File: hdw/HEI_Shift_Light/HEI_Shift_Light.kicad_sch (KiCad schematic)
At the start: 0 parts

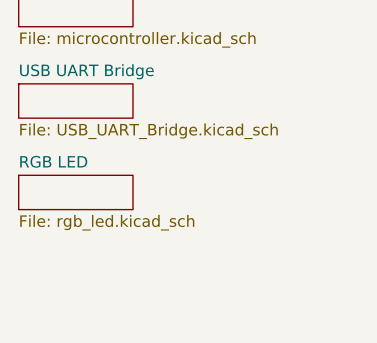
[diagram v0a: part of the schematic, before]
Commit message: moved GND connections to mount holes, updated gitignore
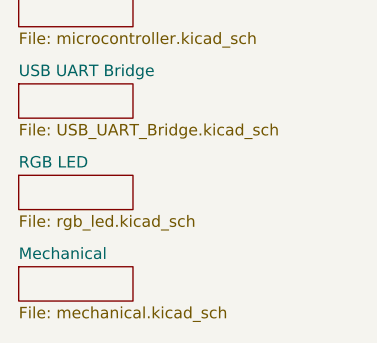
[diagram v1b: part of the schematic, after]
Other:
- added sheet Mechanical (mechanical.kicad_sch)
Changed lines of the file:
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@@
+	)
+	(sheet
+		(at 36.83 109.22)
+		(size 12.7 3.81)
+		(exclude_from_sim no)
+		(in_bom yes)
+		(on_board yes)
+		(dnp no)
+		(fields_autoplaced yes)
+		(stroke
+			(width 0.1524)
+			(type solid)
+		)
+		(fill
+			(color 0 0 0 0)
+		)
+		(property "Sheetname" "Mechanical"
+			(at 36.83 108.5084 0)
+			(show_name no)
+			(do_not_autoplace no)
+			(effects
+				(font
+					(size 1.27 1.27)
+				)
+				(justify left bottom)
+			)
+		)
+		(property "Sheetfile" "mechanical.kicad_sch"
+			(at 36.83 113.6146 0)
+			(show_name no)
+			(do_not_autoplace no)
+			(effects
+				(font
+					(size 1.27 1.27)
+				)
+				(justify left top)
+			)
+		)
+		(instances
+			(project "HEI_Shift_Light"
+				(path "/288c8230-69eb-4ad9-929d-f4630114196f"
+					(page "8")
+				)
+			)
+		)
 	)
 	(sheet

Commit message: updated a lot of font, table of contents
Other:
- note added: "01 - Root"
- note added: "02 - Input Power"
- note added: "03 - 5V Power Supply"
- note added: "04 - Input Signal"
- note added: "05 - Microcontroller"
- note added: "06 - USB UART Bridge"
- note added: "07 - RGB LED"
- note added: "08 - Mechanical"
- note added: "HEI Shift Light"
